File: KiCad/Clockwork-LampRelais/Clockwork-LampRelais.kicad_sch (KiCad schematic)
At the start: 15 parts, among them J1 Lamp, J2 to Proj. Board, K1 FINDER-40.11-2016, Q1 SS8050, Q2 SS8050, U1 LMC555xM

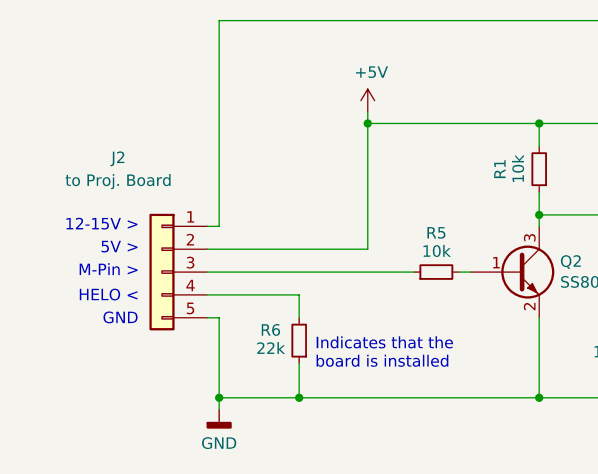
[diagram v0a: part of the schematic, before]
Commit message: Adding the 6th pin to the Lamp Relay Schematic
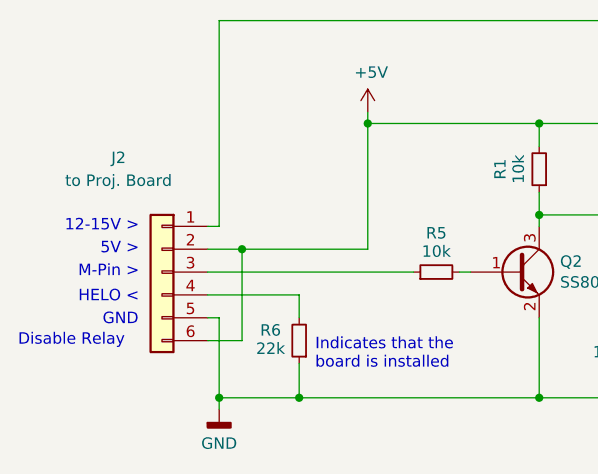
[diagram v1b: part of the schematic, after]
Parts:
- J2: symbol Connector_Generic:Conn_01x05 -> Connector_Generic:Conn_01x06
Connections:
- net +5V: now also J2.6 (Pin_6)
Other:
- note added: "Disable Relay"
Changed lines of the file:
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@@
+	)
+	(junction
+		(at 46.99 78.74)
+		(diameter 0)
+		(color 0 0 0 0)
 	)
 	(junction
@@
 	(wire
 		(pts
-			(xy 43.18 78.74) (xy 60.96 78.74)
+			(xy 43.18 78.74) (xy 46.99 78.74)
 		)
 		(stroke
@@
 	(wire
 		(pts
+			(xy 43.18 88.9) (xy 46.99 88.9)
+		)
+		(stroke
+			(width 0)
+			(type default)
+		)
+	)
+	(wire
+		(pts
 			(xy 91.44 80.01) (xy 91.44 86.36)
 		)
@@
 	(wire
 		(pts
+			(xy 46.99 88.9) (xy 46.99 78.74)
+		)
+		(stroke
+			(width 0)
+			(type default)
+		)
+	)
+	(wire
+		(pts
+			(xy 46.99 78.74) (xy 60.96 78.74)
+		)
+		(stroke
+			(width 0)
+			(type default)
+		)
+	)
+	(wire
+		(pts
 			(xy 133.35 68.58) (xy 133.35 64.77)
 		)
@@
 			(width 0)
 			(type default)
+		)
+	)
+	(text "Disable Relay"
+		(exclude_from_sim no)
+		(at 22.098 88.9 0)
+		(effects
+			(font
+				(size 1.27 1.27)
+			)
+			(justify left)
 		)
 	)
@@
 	)
 	(symbol
-		(lib_id "Connector_Generic:Conn_01x05")
+		(lib_id "Connector_Generic:Conn_01x06")
 		(at 38.1 81.28 0)
 		(mirror y)
@@
 			)
 		)
-		(property "Description" "Generic connector, single row, 01x05, script generated (kicad-library-utils/schlib/autogen/connector/)"
+		(property "Description" "Generic connector, single row, 01x06, script generated (kicad-library-utils/schlib/autogen/connector/)"
 			(at 38.1 81.28 0)
 			(effects
@@
 		(pin "5"
 		)
+		(pin "6"
+		)
 		(instances
